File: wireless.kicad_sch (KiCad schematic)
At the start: 16 parts, among them J1301 u.FL, U1301 LBEE5KL1YN-814

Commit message: Add series termination, assign netclasses, fill schemas' descriptions
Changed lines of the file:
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@@
 		(members "WLAN.D[0..3]" "WLAN.CMD" "WLAN.CLK" "WLAN.REG_ON" "WLAN.HOST_WKUP")
+	)
+	(text_box "Notes"
+		(exclude_from_sim no)
+		(at 12.7 251.46 0)
+		(size 285.75 33.02)
+		(margins 0.9525 2 0.9525 0.9525)
+		(stroke
+			(width 0)
+			(type solid)
+		)
+		(fill
+			(type none)
+		)
+		(effects
+			(font
+				(size 5.08 5.08)
+				(thickness 1.016)
+				(bold yes)
+			)
+			(justify top)
+		)
 	)
 	(text_box "11. Wireless"
@@
 		)
 	)
+	(text_box "WLAN and Bluetooth 5"
+		(exclude_from_sim no)
+		(at 12.7 50.8 0)
+		(size 393.7 200.66)
+		(margins 0.9525 2 0.9525 0.9525)
+		(stroke
+			(width 0)
+			(type solid)
+		)
+		(fill
+			(type none)
+		)
+		(effects
+			(font
+				(size 5.08 5.08)
+				(thickness 1.016)
+				(bold yes)
+			)
+			(justify top)
+		)
+	)
 	(junction
 		(at 184.15 226.06)
@@
 		)
 	)
+	(rule_area
+		(polyline
+			(pts
+				(xy 290.83 168.91) (xy 290.83 176.53) (xy 254 176.53) (xy 254 168.91)
+			)
+			(stroke
+				(width 0)
+				(type dash)
+			)
+			(fill
+				(type none)
+			)
+		)
+	)
+	(netclass_flag ""
+		(length 2.54)
+		(shape round)
+		(at 273.05 168.91 0)
+		(fields_autoplaced yes)
+		(effects
+			(font
+				(size 1.27 1.27)
+			)
+			(justify left bottom)
+		)
+		(property "Netclass" "ANT"
+			(at 273.7485 166.37 0)
+			(effects
+				(font
+					(size 1.27 1.27)
+				)
+				(justify left)
+			)
+		)
+		(property "Component Class" ""
+			(at -26.67 3.81 0)
+			(effects
+				(font
+					(size 1.27 1.27)
+					(italic yes)
+				)
+			)
+		)
+	)

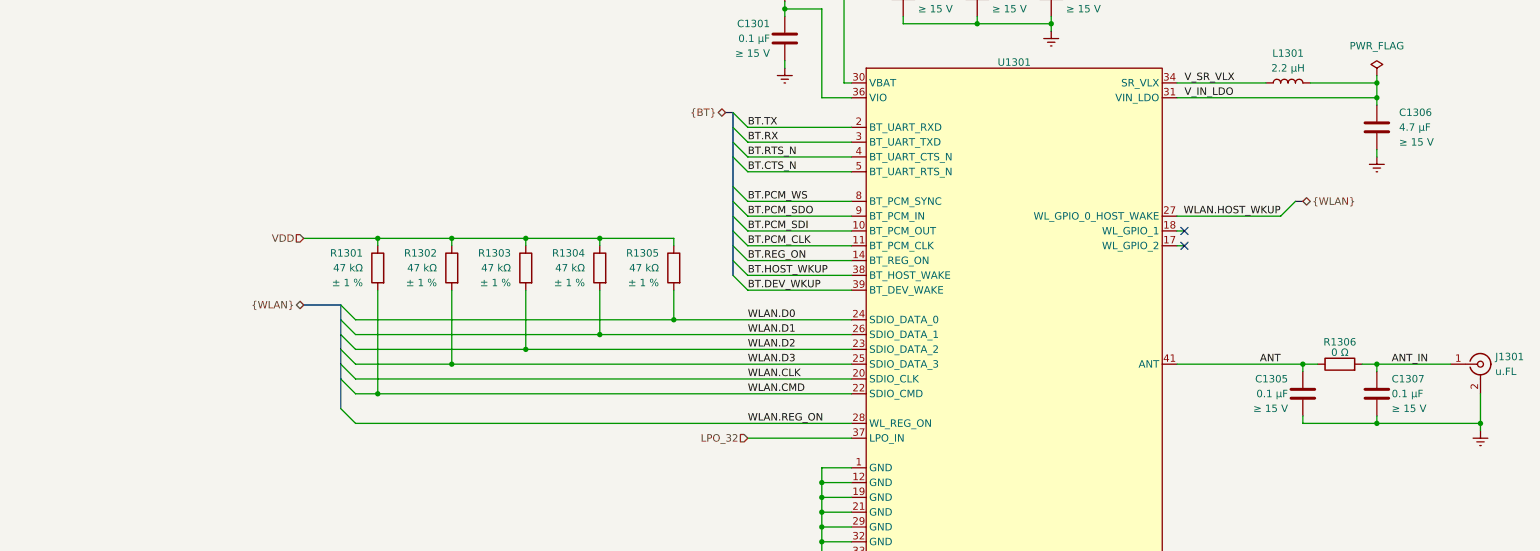
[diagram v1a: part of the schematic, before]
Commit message: Add series termination, refactor schematics
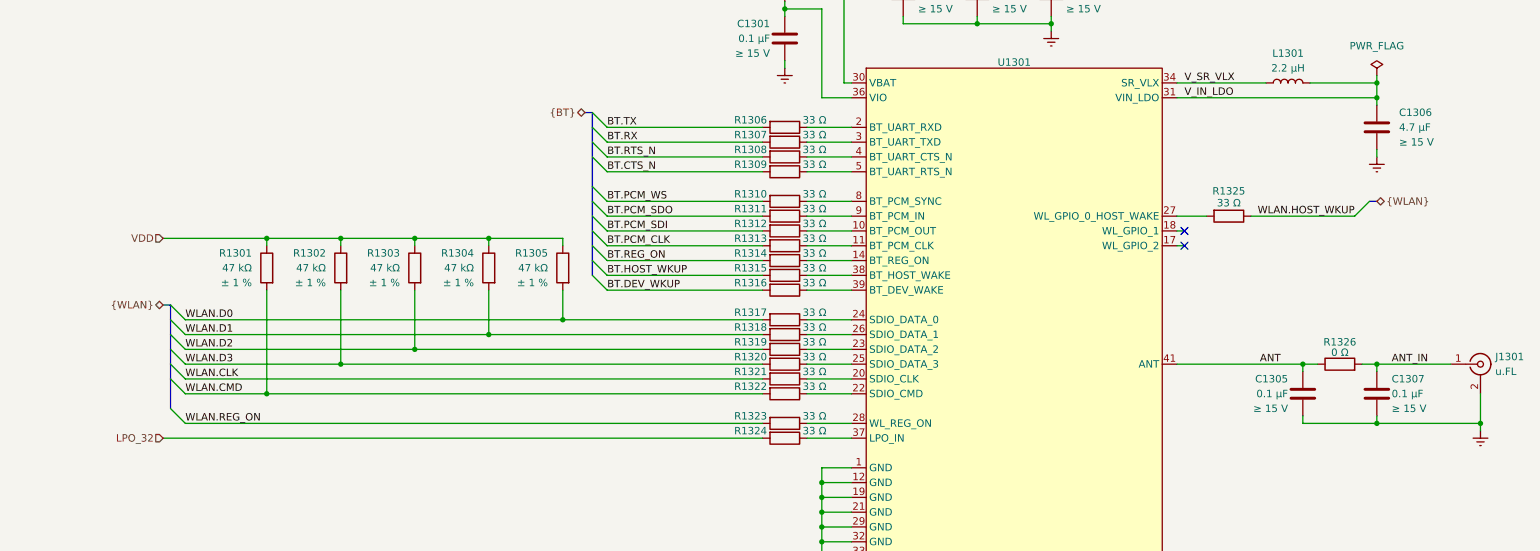
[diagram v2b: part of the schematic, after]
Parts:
- added R1306, R1307, R1308, R1309, R1310, R1311, R1312, R1313, R1314, R1315, R1316, R1317, R1318, R1319, R1320, R1321, R1322, R1323, R1324, R1325: 33 Ω, perfect_footprints:R_0402_1005Metric, symbol Device:R
- renumbered R1306 to R1326
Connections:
- net BT.CTS_N: now also R1309.2; no longer U1301.5 (BT_UART_RTS_N)
- net BT.DEV_WKUP: now also R1316.2; no longer U1301.39 (BT_DEV_WAKE)
- net BT.HOST_WKUP: now also R1315.2; no longer U1301.38 (BT_HOST_WAKE)
- net BT.PCM_CLK: now also R1313.2; no longer U1301.11 (BT_PCM_CLK)
- net BT.PCM_SDI: now also R1312.2; no longer U1301.10 (BT_PCM_OUT)
- net BT.PCM_SDO: now also R1311.2; no longer U1301.9 (BT_PCM_IN)
- net BT.PCM_WS: now also R1310.2; no longer U1301.8 (BT_PCM_SYNC)
- net BT.REG_ON: now also R1314.2; no longer U1301.14 (BT_REG_ON)
- net BT.RTS_N: now also R1308.2; no longer U1301.4 (BT_UART_CTS_N)
- net BT.RX: now also R1307.2; no longer U1301.3 (BT_UART_TXD)
- net BT.TX: now also R1306.2; no longer U1301.2 (BT_UART_RXD)
- net LPO_32: now also R1324.2; no longer U1301.37 (LPO_IN)
- net WLAN.CLK: now also R1321.2; no longer U1301.20 (SDIO_CLK)
- net WLAN.CMD: now also R1322.2; no longer U1301.22 (SDIO_CMD)
- net WLAN.D0: now also R1317.2; no longer U1301.24 (SDIO_DATA_0)
- net WLAN.D1: now also R1318.2; no longer U1301.26 (SDIO_DATA_1)
- net WLAN.D2: now also R1319.2; no longer U1301.23 (SDIO_DATA_2)
- net WLAN.D3: now also R1320.2; no longer U1301.25 (SDIO_DATA_3)
- net WLAN.HOST_WKUP: now also R1325.1; no longer U1301.27 (WL_GPIO_0_HOST_WAKE)
- net WLAN.REG_ON: now also R1323.2; no longer U1301.28 (WL_REG_ON)
- new net: R1317.1, U1301.24 (SDIO_DATA_0)
- new net: R1308.1, U1301.4 (BT_UART_CTS_N)
- new net: R1316.1, U1301.39 (BT_DEV_WAKE)
- new net: R1323.1, U1301.28 (WL_REG_ON)
- new net: R1309.1, U1301.5 (BT_UART_RTS_N)
- new net: R1312.1, U1301.10 (BT_PCM_OUT)
- new net: R1313.1, U1301.11 (BT_PCM_CLK)
- new net: R1314.1, U1301.14 (BT_REG_ON)
- new net: R1306.1, U1301.2 (BT_UART_RXD)
- new net: R1321.1, U1301.20 (SDIO_CLK)
- new net: R1322.1, U1301.22 (SDIO_CMD)
- new net: R1319.1, U1301.23 (SDIO_DATA_2)
- new net: R1320.1, U1301.25 (SDIO_DATA_3)
- new net: R1318.1, U1301.26 (SDIO_DATA_1)
- new net: R1325.2, U1301.27 (WL_GPIO_0_HOST_WAKE)
- new net: R1307.1, U1301.3 (BT_UART_TXD)
- new net: R1324.1, U1301.37 (LPO_IN)
- new net: R1315.1, U1301.38 (BT_HOST_WAKE)
- new net: R1310.1, U1301.8 (BT_PCM_SYNC)
- new net: R1311.1, U1301.9 (BT_PCM_IN)
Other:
- moved on the sheet: R1301, R1302, R1303, R1304, R1305

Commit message: Refactor symbol properties
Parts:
- C1303, C1306: DigiKey Part Number 490-7205-1-ND -> (none)
- R1306, R1307, R1308, R1309, R1310, R1311, R1312, R1313, R1314, R1315, R1316, R1317, R1318, R1319, R1320, R1321, R1322, R1323, R1324, R1325: DigiKey Part Number 732-560112110020CT-ND -> (none)

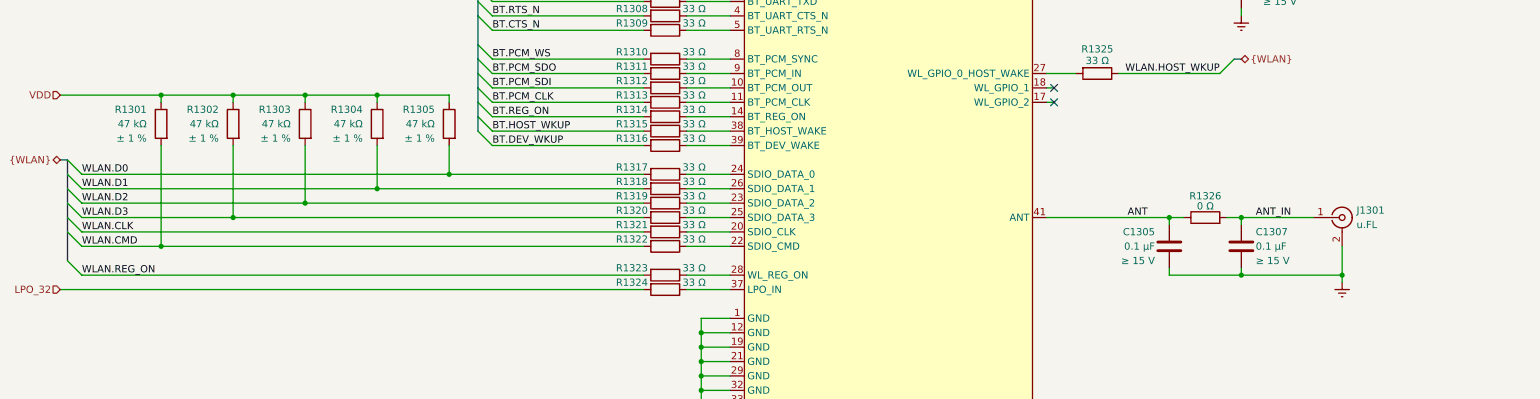
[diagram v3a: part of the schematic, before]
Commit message: Refactor SDMMC, UI, Wirelessg
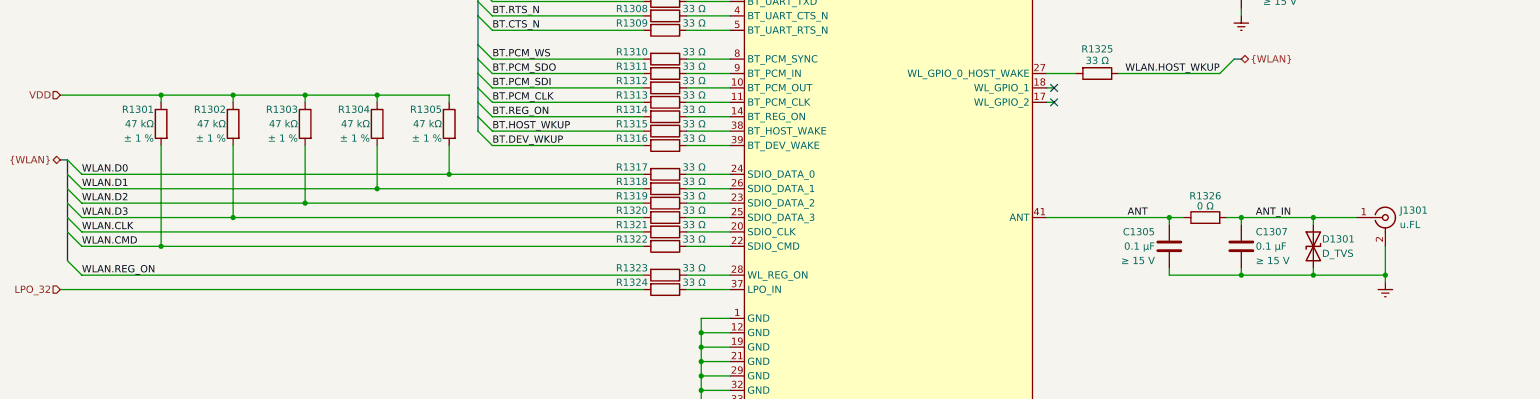
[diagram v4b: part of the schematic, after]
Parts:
- added D1301: D_TVS, symbol Device:D_TVS
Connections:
- net ANT_IN: now also D1301.1 (A1)
- net GND: now also D1301.2 (A2)
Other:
- moved on the sheet: J1301
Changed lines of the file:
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@@
 	)
 	(junction
+		(at 292.1 185.42)
+		(diameter 0)
+		(color 0 0 0 0)
+	)
+	(junction
 		(at 184.15 215.9)
 		(diameter 0)
@@
 	)
 	(junction
+		(at 304.8 185.42)
+		(diameter 0)
+		(color 0 0 0 0)
+	)
+	(junction
 		(at 184.15 200.66)
 		(diameter 0)
@@
 	)
 	(junction
-		(at 297.18 185.42)
+		(at 292.1 175.26)
 		(diameter 0)
 		(color 0 0 0 0)
@@
 	(wire
 		(pts
+			(xy 292.1 175.26) (xy 292.1 176.53)
+		)
+		(stroke
+			(width 0)
+			(type default)
+		)
+	)
+	(wire
+		(pts
 			(xy 184.15 226.06) (xy 184.15 227.33)
 		)
@@
 	(wire
 		(pts
-			(xy 297.18 185.42) (xy 297.18 186.69)
+			(xy 304.8 185.42) (xy 304.8 186.69)
 		)
 		(stroke
@@
 	(wire
 		(pts
+			(xy 292.1 184.15) (xy 292.1 185.42)
+		)
+		(stroke
+			(width 0)
+			(type default)
+		)
+	)
+	(wire
+		(pts
 			(xy 198.12 106.68) (xy 187.96 106.68)
 		)
@@
 	(wire
 		(pts
-			(xy 279.4 185.42) (xy 297.18 185.42)
+			(xy 279.4 185.42) (xy 292.1 185.42)
 		)
 		(stroke
@@
 	(wire
 		(pts
-			(xy 297.18 180.34) (xy 297.18 185.42)
+			(xy 292.1 175.26) (xy 299.72 175.26)
+		)
+		(stroke
+			(width 0)
+			(type default)
+		)
+	)
+	(wire
+		(pts
+			(xy 304.8 180.34) (xy 304.8 185.42)
 		)
 		(stroke
@@
 	(wire
 		(pts
+			(xy 292.1 185.42) (xy 304.8 185.42)
+		)
+		(stroke
+			(width 0)
+			(type default)
+		)
+	)
+	(wire
+		(pts
 			(xy 210.82 106.68) (xy 223.52 106.68)
 		)
@@
 	(symbol
 		(lib_id "Connector:Conn_Coaxial")
-		(at 297.18 175.26 0)
+		(at 304.8 175.26 0)
 		(unit 1)
 		(exclude_from_sim no)
@@
 		(dnp no)
 		(property "Reference" "J1301"
-			(at 299.72 173.99 0)
+			(at 307.34 173.99 0)
 			(effects
 				(font
@@
 		)
 		(property "Value" "u.FL"
-			(at 299.72 176.53 0)
+			(at 307.34 176.53 0)
 			(effects
 				(font
@@
 		)
 		(property "Footprint" ""
-			(at 297.18 175.26 0)
+			(at 304.8 175.26 0)
 			(effects
 				(font
@@
 		)
 		(property "Datasheet" "~"
-			(at 297.18 175.26 0)
+			(at 304.8 175.26 0)
 			(effects
 				(font
@@
 		)
 		(property "Description" "coaxial connector (BNC, SMA, SMB, SMC, Cinch/RCA, LEMO, ...)"
-			(at 297.18 175.26 0)
+			(at 304.8 175.26 0)
 			(effects
 				(font
@@
 		(dnp no)
 		(property "Reference" "R1302"
-			(at 99.06 156.21 0)
+			(at 100.33 156.21 0)
 			(effects
 				(font
@@
 		)
 		(property "Value" "47 kΩ"
-			(at 99.06 158.75 0)
+			(at 100.33 158.75 0)
 			(effects
 				(font
@@
 		)
 		(property "Tolerance" "± 1 %"
-			(at 99.06 161.2901 0)
+			(at 100.33 161.2901 0)
 			(effects
 				(font
@@
 		(dnp no)
 		(property "Reference" "R1303"
-			(at 111.76 156.21 0)
+			(at 113.03 156.21 0)
 			(effects
 				(font
@@
 		)
 		(property "Value" "47 kΩ"
-			(at 111.76 158.75 0)
+			(at 113.03 158.75 0)
 			(effects
 				(font
@@
 		)
 		(property "Tolerance" "± 1 %"
-			(at 111.76 161.2901 0)
+			(at 113.03 161.2901 0)
 			(effects
 				(font
@@
 		(dnp no)
 		(property "Reference" "R1304"
-			(at 124.46 156.21 0)
+			(at 125.73 156.21 0)
 			(effects
 				(font
@@
 		)
 		(property "Value" "47 kΩ"
-			(at 124.46 158.75 0)
+			(at 125.73 158.75 0)
 			(effects
 				(font
@@
 		)
 		(property "Tolerance" "± 1 %"
-			(at 124.46 161.2901 0)
+			(at 125.73 161.2901 0)
 			(effects
 				(font
@@
 	)
 	(symbol
+		(lib_id "Device:D_TVS")
+		(at 292.1 180.34 90)
+		(mirror x)
+		(unit 1)
+		(exclude_from_sim no)
+		(in_bom yes)
+		(on_board yes)
+		(dnp no)
+		(property "Reference" "D1301"
+			(at 293.624 179.07 90)
+			(effects
+				(font
+					(size 1.27 1.27)
+				)
+				(justify right)
+			)
+		)
+		(property "Value" "D_TVS"
+			(at 293.624 181.61 90)
+			(effects
+				(font
+					(size 1.27 1.27)
+				)
+				(justify right)
+			)
+		)
+		(property "Footprint" ""
+			(at 292.1 180.34 0)
+			(effects
+				(font
+					(size 1.27 1.27)
+				)
+				(hide yes)
+			)
+		)
+		(property "Datasheet" "~"
+			(at 292.1 180.34 0)
+			(effects
+				(font
+					(size 1.27 1.27)
+				)
+				(hide yes)
+			)
+		)
+		(property "Description" "Bidirectional transient-voltage-suppression diode"
+			(at 292.1 180.34 0)
+			(effects
+				(font
+					(size 1.27 1.27)
+				)
+				(hide yes)
+			)
+		)
+		(pin "1"
+		)
+		(pin "2"
+		)
+		(instances
+			(project "linux-sbc"
+				(path "/fa11a02f-8043-4153-ab69-88d766503017/24c9b83b-271d-4c51-b843-406c618d8ce8"
+					(reference "D1301")
+					(unit 1)
+				)
+			)
+		)
+	)
+	(symbol
 		(lib_id "Device:R")
 		(at 177.8 187.96 270)
@@
 		(dnp no)
 		(property "Reference" "R1305"
-			(at 137.16 156.21 0)
+			(at 138.43 156.21 0)
 			(effects
 				(font
@@
 		)
 		(property "Value" "47 kΩ"
-			(at 137.16 158.75 0)
+			(at 138.43 158.75 0)
 			(effects
 				(font
@@
 		)
 		(property "Tolerance" "± 1 %"
-			(at 137.16 161.2901 0)
+			(at 138.43 161.2901 0)
 			(effects
 				(font
@@
 		(dnp no)
 		(property "Reference" "R1301"
-			(at 86.36 156.21 0)
+			(at 87.63 156.21 0)
 			(effects
 				(font
@@
 		)
 		(property "Value" "47 kΩ"
-			(at 86.36 158.75 0)
+			(at 87.63 158.75 0)
 			(effects
 				(font
@@
 		)
 		(property "Tolerance" "± 1 %"
-			(at 86.36 161.2901 0)
+			(at 87.63 161.2901 0)
 			(effects
 				(font
@@
 	(symbol
 		(lib_id "power:Earth")
-		(at 297.18 186.69 0)
+		(at 304.8 186.69 0)
 		(unit 1)
 		(exclude_from_sim no)
@@
 		(fields_autoplaced yes)
 		(property "Reference" "#PWR01306"
-			(at 297.18 193.04 0)
+			(at 304.8 193.04 0)
 			(effects
 				(font
@@
 		)
 		(property "Value" "GND"
-			(at 297.18 191.77 0)
+			(at 304.8 191.77 0)
 			(effects
 				(font
@@
 		)
 		(property "Footprint" ""
-			(at 297.18 186.69 0)
+			(at 304.8 186.69 0)
 			(effects
 				(font
@@
 		)
 		(property "Datasheet" "~"
-			(at 297.18 186.69 0)
+			(at 304.8 186.69 0)
 			(effects
 				(font
@@
 		)
 		(property "Description" "Power symbol creates a global label with name \"Earth\""
-			(at 297.18 186.69 0)
+			(at 304.8 186.69 0)
 			(effects
 				(font
